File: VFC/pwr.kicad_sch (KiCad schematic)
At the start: 47 parts, among them IC1 MP1584EN-LF-Z, IC2 MP1584EN-LF-Z, P1 USB_C_Plug_USB2.0, Q1 AO3400A, U10 USBLC6-2SC6

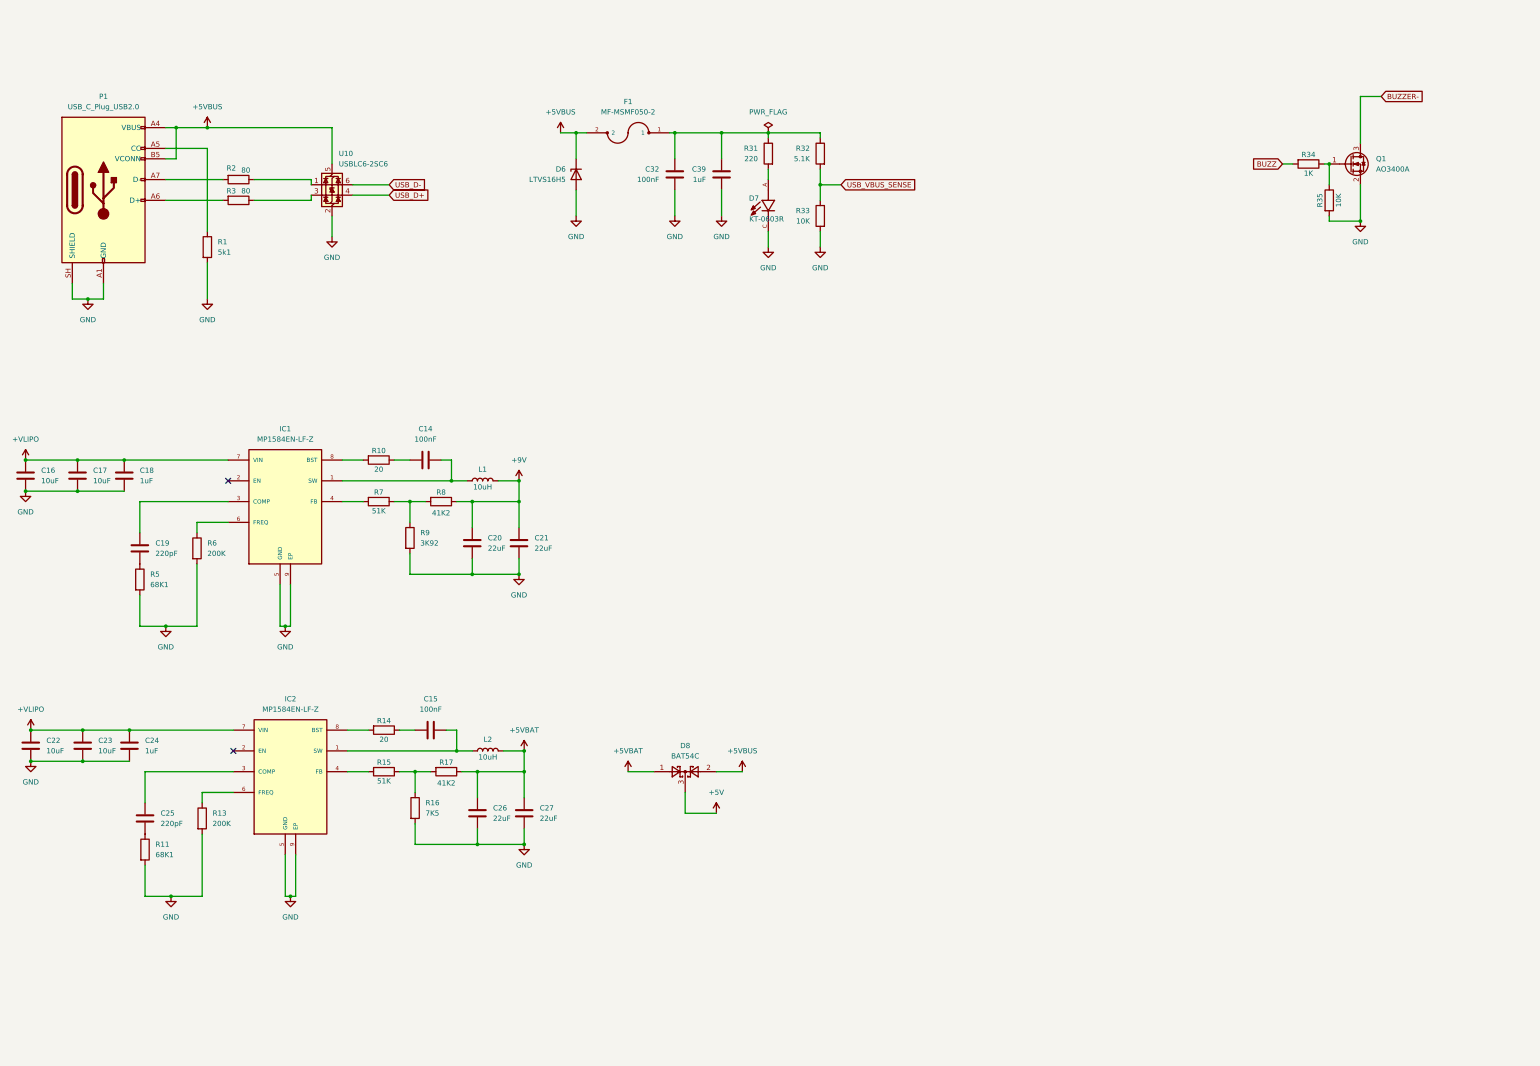
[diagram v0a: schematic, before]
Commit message: VFC PCB components placements complete
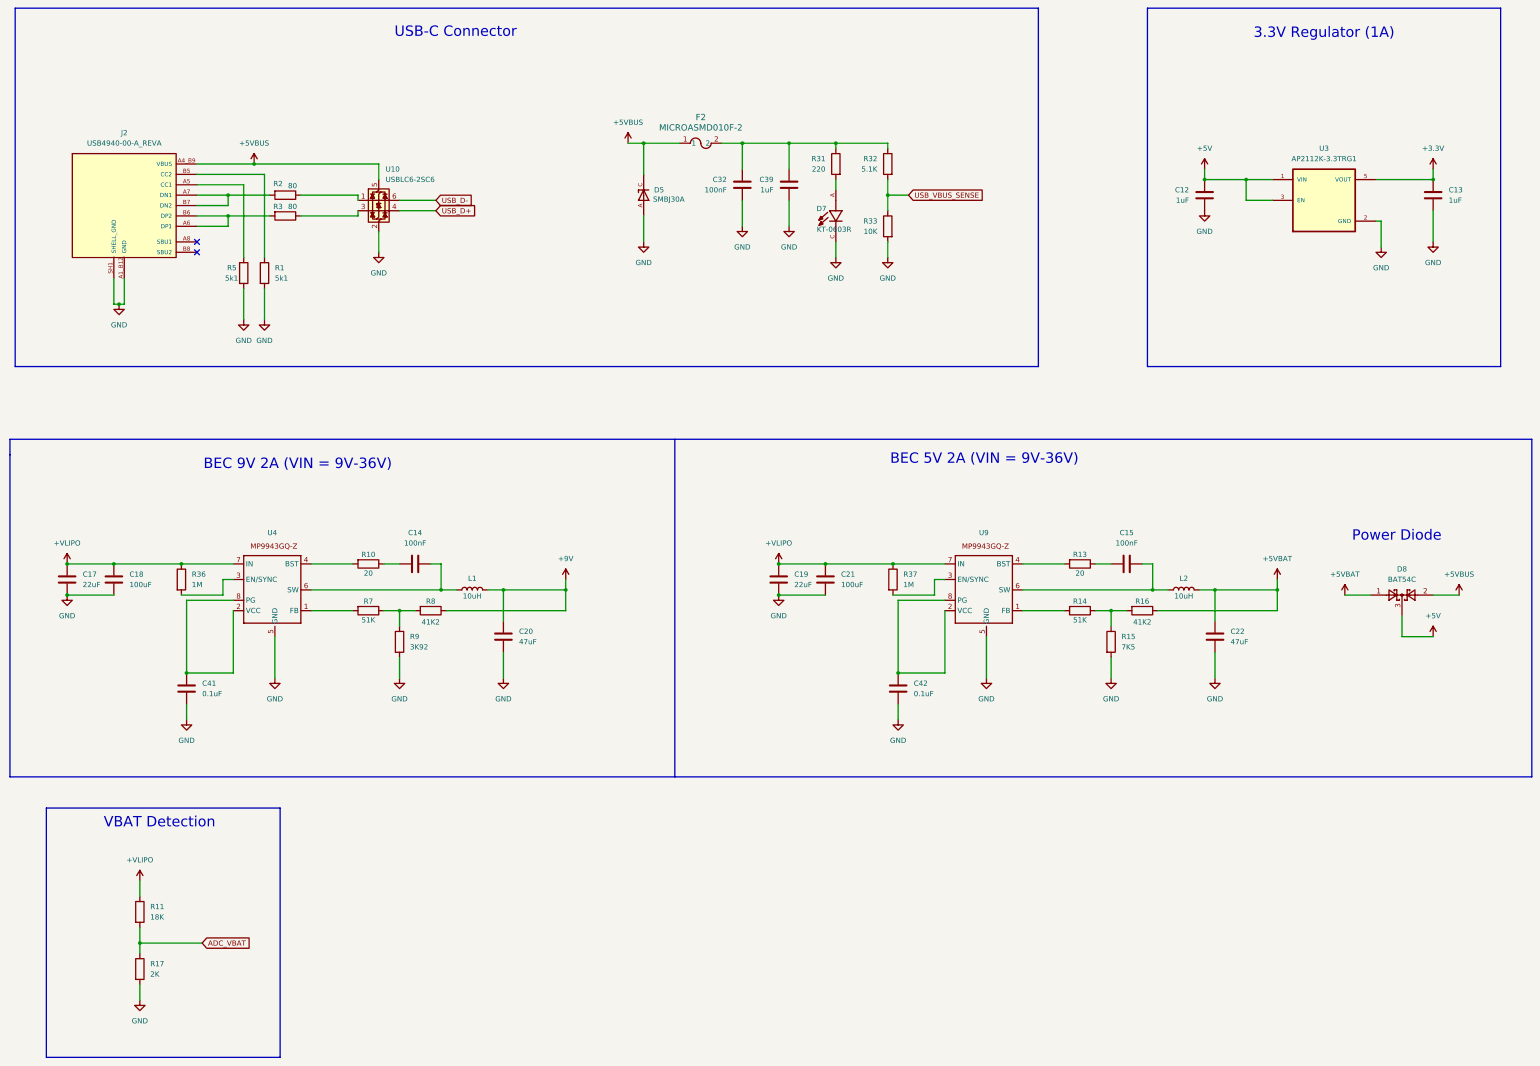
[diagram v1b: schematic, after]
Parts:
- removed C16, C23: 10uF, Capacitor_SMD:C_0402_1005Metric, symbol Device:C
- removed C24: 1uF, Capacitor_SMD:C_0402_1005Metric, symbol Device:C
- removed C25: 220pF, Capacitor_SMD:C_0402_1005Metric, symbol Device:C
- removed C26, C27: 22uF, Capacitor_SMD:C_0402_1005Metric, symbol Device:C
- removed D6: LTVS16H5, Diode_SMD:D_SOD-523, symbol Diode:ESD5Zxx
- removed F1: MF-MSMF050-2, MF-MSMF050-2:FUSM4632X85, symbol MF-MSMF050-2:MF-MSMF050-2
- removed IC1, IC2: MP1584EN-LF-Z, MP1584EN-LF-Z:SOIC127P600X170-9N, symbol MP1584EN-LF-Z:MP1584EN-LF-Z
- removed P1: USB_C_Plug_USB2.0, Connector_USB:USB_C_Receptacle_HRO_TYPE-C-31-M-12, symbol Connector:USB_C_Plug_USB2.0
- removed Q1: AO3400A, Package_TO_SOT_SMD:SOT-23, symbol Transistor_FET:AO3400A
- removed R34: 1K, Resistor_SMD:R_0402_1005Metric, symbol Device:R
- removed R35: 10K, Resistor_SMD:R_0402_1005Metric, symbol Device:R
- removed R6: 200K, Resistor_SMD:R_0402_1005Metric, symbol Device:R
- added C12, C13: 1uF, Capacitor_SMD:C_0402_1005Metric, symbol Device:C
- added C41, C42: 0.1uF, Capacitor_SMD:C_0402_1005Metric, symbol Device:C
- added D5: SMBJ30A, SMBJ30A:DIOM4336X265N, symbol SMBJ30A:SMBJ30A
- added F2: MICROASMD010F-2, MICROASMD010F-2:FUSE_MICROASMD010F_LTF, symbol MICROASMD010F-2:MICROASMD010F-2
- added J2: USB4940-00-A_REVA, USB4940-00-A_REVA:GCT_USB4940-00-A_REVA, symbol USB4940-00-A_REVA:USB4940-00-A_REVA
- added R36, R37: 1M, Resistor_SMD:R_0402_1005Metric, symbol Device:R
- added U3: AP2112K-3.3TRG1, AP2112K-3.3TRG1:SOT95P285X140-5N, symbol AP2112K-3.3TRG1:AP2112K-3.3TRG1
- added U4, U9: (no value), MP9943GQ-Z:QFN-8_MP9943_MNP, symbol MP9943GQ-Z:MP9943GQ-Z
- C17: value 10uF -> 22uF; footprint Capacitor_SMD:C_0402_1005Metric -> Capacitor_SMD:C_0603_1608Metric
- C18: value 1uF -> 100uF; footprint Capacitor_SMD:C_0402_1005Metric -> Capacitor_SMD:C_0603_1608Metric
- C19: value 220pF -> 22uF; footprint Capacitor_SMD:C_0402_1005Metric -> Capacitor_SMD:C_0603_1608Metric
- C20: value 22uF -> 47uF; footprint Capacitor_SMD:C_0402_1005Metric -> Capacitor_SMD:C_0603_1608Metric
- C21: value 22uF -> 100uF; footprint Capacitor_SMD:C_0402_1005Metric -> Capacitor_SMD:C_0603_1608Metric
- C22: value 10uF -> 47uF; footprint Capacitor_SMD:C_0402_1005Metric -> Capacitor_SMD:C_0603_1608Metric
- C32, C39: footprint (none) -> Capacitor_SMD:C_0402_1005Metric
- R11: value 68K1 -> 18K
- R13: value 200K -> 20
- R14: value 20 -> 51K
- R15: value 51K -> 7K5
- R16: value 7K5 -> 41K2
- R17: value 41K2 -> 2K
- R31, R32, R33: footprint (none) -> Resistor_SMD:R_0402_1005Metric
- R5: value 68K1 -> 5k1
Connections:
- net +5V: now also C12.1, U3.1 (VIN), U3.3 (EN)
- net +5VBAT: now also C22.1, R16.1; no longer R17.1
- net +5VBUS: now also D5.C, F2.1, J2.A4_B9 (VBUS), J2.B4_A9 (VBUS)
- net +9V: no longer C21.1
- net +VLIPO: now also C19.1, C21.1, R11.1, R36.1, R37.1, U4.7 (IN), U9.7 (IN); no longer C22.1
- net GND: now also C19.2, R15.2, R17.2, C12.2, C13.2, C41.2, C42.2, D5.A, J2.A1_B12 (GND), J2.B1_A12 (GND), J2.SH1 (SHELL_GND), J2.SH2 (SHELL_GND), J2.SH3 (SHELL_GND), J2.SH4 (SHELL_GND), U3.2 (GND), U4.5 (GND), U9.5 (GND); no longer R11.2, R13.2, R16.2
- net at R10.2: now also U4.4 (BST)
- net at R1.1: now also J2.B5 (CC2)
- net at C15.2: now also R13.1; no longer R14.1
- net at R14.2: now also U9.1 (FB)
- net at R7.2: now also U4.1 (FB)
- net at C14.1, L1.1: now also U4.6 (SW)
- net at R3.2: now also J2.A6 (DP1), J2.B6 (DP2)
- net at R5.1: now also J2.A5 (CC1); no longer C19.2
- net at R2.2: now also J2.A7 (DN1), J2.B7 (DN2)
- net at C15.1, L2.1: now also U9.6 (SW)
- net at C32.1, C39.1, R31.1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: now also F2.2
- new net: C42.1, U9.2 (VCC), U9.8 (PG)
- new net: R37.2, U9.3 (EN/SYNC)
- new net: R13.2, U9.4 (BST)
- new net: C41.1, U4.2 (VCC), U4.8 (PG)
- new net: R36.2, U4.3 (EN/SYNC)
- new net: R14.1, R15.1, R16.2
- new net +3.3V: C13.1, U3.5 (VOUT)
- new net ADC_VBAT: R11.2, R17.1
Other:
- note added: "3.3V Regulator (1A)"
- note added: "BEC 5V 2A (VIN = 9V-36V)"
- note added: "BEC 9V 2A (VIN = 9V-36V)"
- note added: "Power Diode"
- note added: "USB-C Connector"
- note added: "VBAT Detection"
- moved on the sheet: C14, C17, C18, C20, C32, C39, D7, D8, L1, R1, R10, R2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

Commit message: VFC PCB traces update
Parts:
- removed U3: AP2112K-3.3TRG1, AP2112K-3.3TRG1:SOT95P285X140-5N, symbol AP2112K-3.3TRG1:AP2112K-3.3TRG1
- added C24, C25: 1uF, Capacitor_SMD:C_0402_1005Metric, symbol Device:C
- added FL2: 220 Ohms @ 100 MHz, BLM18PG221SN1D:BEADC1608X95N, symbol BLM18PG221SN1D:BLM18PG221SN1D
- added U11: AP7361C-FGE-7, AP7361C-FGE-7:SON65P300X300X63-9N, symbol AP7361C-FGE-7:AP7361C-FGE-7
- added U3: NCP167BMX330TBG, NCP167BMX330TBG:VREG_NCP167BMX330TBG, symbol NCP167BMX330TBG:NCP167BMX330TBG
- C12, C13: value 1uF -> 4.7uF
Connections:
- net +3.3V: now also U11.1 (OUT)
- net +5V: now also C24.1, U11.5 (EN), U11.8 (IN), U3.3 (EN), U3.4 (IN)
- net GND: now also C24.2, C25.2, U11.4 (GND), U11.9 (GND), U3.2 (GND), U3.5 (EPAD)
- new net: C25.1, FL2.1, U3.1 (OUT)
- new net: U11.2 (NC), U11.6 (NC), U11.7 (NC)
- new net +3.3VA: FL2.2
- no-connect marks 2 -> 3
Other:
- note added: "3.3V Analog Regulator (700mA)"
- moved on the sheet: C12, C13
